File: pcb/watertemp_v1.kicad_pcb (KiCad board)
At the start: 2 copper layers, 56 x 90 mm, 56 parts, among them J1 RN2483 Ext, J2 SWD, J3 I2C, J4 UART1, J5 UART0, Q1 Q_PMOS_GSD, U1 LPC11U24FBD48, U2 RN2483, U3 SHT21, U4 LP5907-Q1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

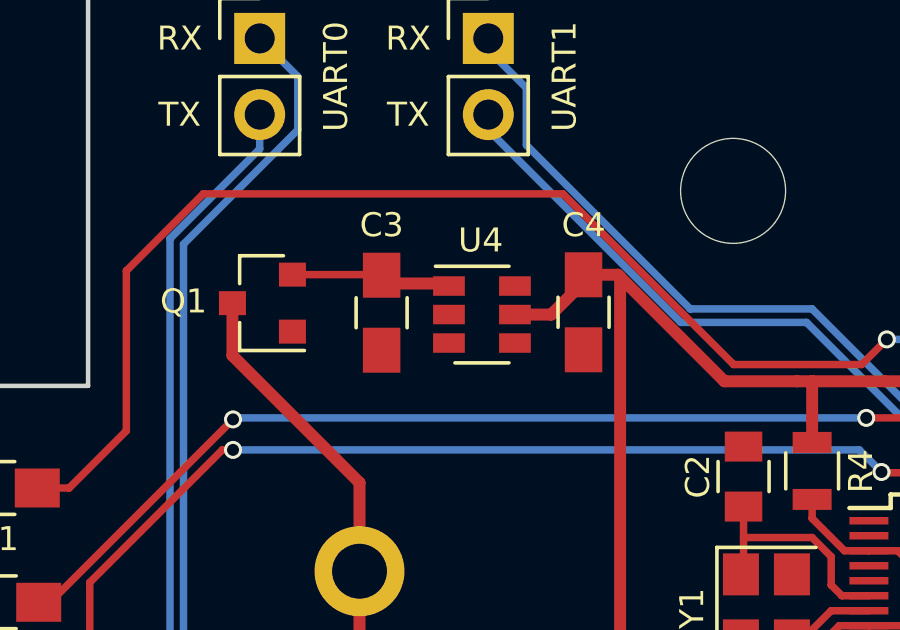
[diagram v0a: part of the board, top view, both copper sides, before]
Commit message: Fix problems with LDO
- Use SOT-23-5 footprint (fixes #9)
- Connect EN to IN
- Connect pin 4 (NC) to GND as recommended in the
  datasheet (section 11.2)
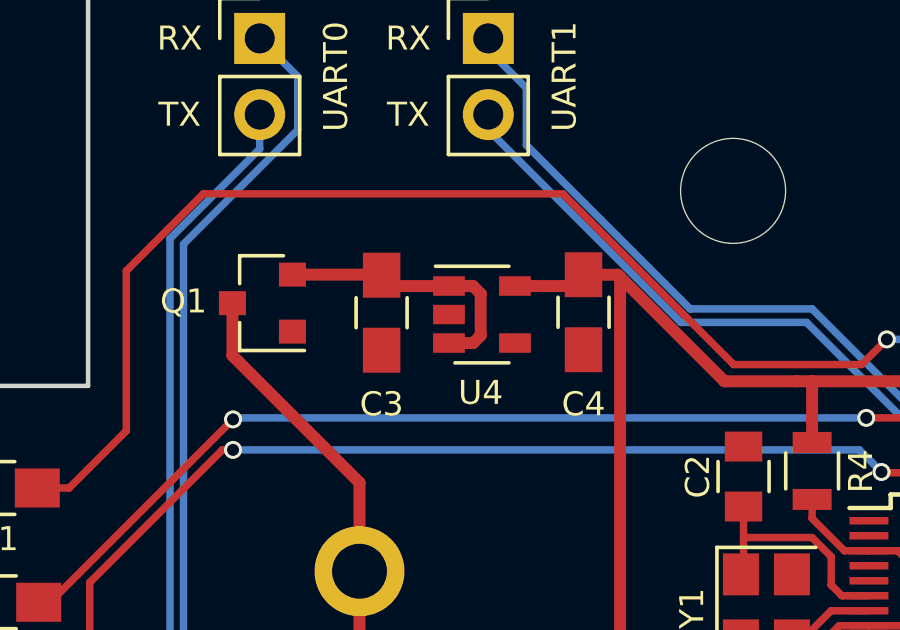
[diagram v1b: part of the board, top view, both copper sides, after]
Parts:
- U4: footprint TO_SOT_Packages_SMD:SOT-23-6 -> TO_SOT_Packages_SMD:SOT-23-5
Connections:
- U4 pad 3: Net-(U4-Pad3) -> Net-(C3-Pad1)
- U4 pad 4: (no net) -> GND
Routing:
- net Net-(C3-Pad1): track 5.35 -> 9.34 mm

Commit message: Routing for voltage divider (fixes #4)
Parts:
- added Q2: Q_DUAL_NMOS_GSD_PMOS_SGD, TSOT_Custom:TSOT26, F.Cu at (63.8, 42.3)
- added R10: 9.30K 0.1%, Resistors_SMD:R_0805, F.Cu at (66.1, 49.3)
- added R11: 10KΩ, Resistors_SMD:R_0805, F.Cu at (68.9, 41.6)
- added R12: 10KΩ, Resistors_SMD:R_0805, F.Cu at (58.1, 43.2)
- added R9: 6.04K 0.1%, Resistors_SMD:R_0805, F.Cu at (66.0, 45.9)
- C3, C4, C5: footprint Capacitors_SMD:C_0805_HandSoldering -> Capacitors_SMD:C_0805
- R1, R2, R3, R6, R7, R8: footprint Resistors_SMD:R_0805_HandSoldering -> Resistors_SMD:R_0805
- moved J4 2.54 mm to (50.8, 42.4)
- moved R1 2.03 mm to (34.9, 57.4)
- moved R2 2.03 mm to (35.0, 61.2)
- moved R3 2.03 mm to (35.0, 65.0)
- moved J5 1.52 mm to (44.2, 42.4)
- moved D1 1.27 mm to (30.7, 57.4)
- moved D3 1.27 mm to (30.7, 65.0)
- moved D2 1.27 mm to (30.7, 61.2)
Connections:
- net Net-(C3-Pad1) renamed VBat
- J2 pad 6: Net-(J2-Pad6) -> (no net)
- J2 pad 7: Net-(J2-Pad7) -> (no net)
- J2 pad 8: Net-(J2-Pad8) -> (no net)
- U1 pad 1: Net-(U1-Pad1) -> (no net)
- U1 pad 10: Net-(U1-Pad10) -> (no net)
- U1 pad 11: Net-(U1-Pad11) -> (no net)
- U1 pad 12: Net-(U1-Pad12) -> (no net)
- U1 pad 13: Net-(U1-Pad13) -> (no net)
- U1 pad 14: Net-(U1-Pad14) -> (no net)
- U1 pad 17: Net-(U1-Pad17) -> (no net)
- U1 pad 18: Net-(U1-Pad18) -> (no net)
- U1 pad 19: Net-(U1-Pad19) -> GND
- U1 pad 2: Net-(U1-Pad2) -> (no net)
- U1 pad 20: Net-(U1-Pad20) -> GND
- U1 pad 21: Net-(U1-Pad21) -> (no net)
- U1 pad 22: Net-(U1-Pad22) -> (no net)
- U1 pad 23: Net-(U1-Pad23) -> (no net)
- U1 pad 24: Net-(U1-Pad24) -> (no net)
- U1 pad 26: Net-(U1-Pad26) -> (no net)
- U1 pad 27: Net-(U1-Pad27) -> (no net)
- U1 pad 28: Net-(U1-Pad28) -> (no net)
- U1 pad 30: Net-(U1-Pad30) -> (no net)
- U1 pad 31: Net-(U1-Pad31) -> (no net)
- U1 pad 32: Net-(U1-Pad32) -> (no net)
- U1 pad 33: Net-(U1-Pad33) -> (no net)
- U1 pad 34: Net-(U1-Pad34) -> (no net)
- U1 pad 35: Net-(U1-Pad35) -> (no net)
- U1 pad 4: Net-(U1-Pad4) -> (no net)
- U1 pad 40: Net-(U1-Pad40) -> (no net)
- U1 pad 42: Net-(U1-Pad42) -> ADC
- U1 pad 43: Net-(U1-Pad43) -> VDivEnable
- U1 pad 9: Net-(U1-Pad9) -> (no net)
- U2 pad 10: Net-(U2-Pad10) -> (no net)
- U2 pad 13: Net-(U2-Pad13) -> (no net)
- U2 pad 14: Net-(U2-Pad14) -> (no net)
- U2 pad 2: Net-(U2-Pad2) -> (no net)
- U2 pad 25: Net-(U2-Pad25) -> (no net)
- U2 pad 3: Net-(U2-Pad3) -> (no net)
- U2 pad 35: Net-(U2-Pad35) -> (no net)
- U2 pad 36: Net-(U2-Pad36) -> (no net)
- U2 pad 37: Net-(U2-Pad37) -> (no net)
- U2 pad 38: Net-(U2-Pad38) -> (no net)
- U2 pad 39: Net-(U2-Pad39) -> (no net)
- U2 pad 4: Net-(U2-Pad4) -> (no net)
- U2 pad 40: Net-(U2-Pad40) -> (no net)
- U2 pad 43: Net-(U2-Pad43) -> (no net)
- U2 pad 44: Net-(U2-Pad44) -> (no net)
- U2 pad 45: Net-(U2-Pad45) -> (no net)
- U2 pad 46: Net-(U2-Pad46) -> (no net)
- U2 pad 5: Net-(U2-Pad5) -> (no net)
- U2 pad 9: Net-(U2-Pad9) -> (no net)
- U3 pad 3: Net-(U3-Pad3) -> (no net)
- U3 pad 4: Net-(U3-Pad4) -> (no net)
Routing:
- net VDivEnable: track 0.00 -> 23.2 mm
- net ADC: track 0.00 -> 16.5 mm, vias 0 -> 2
- net VBat: track 9.34 -> 21.8 mm, vias 0 -> 2
- net Net-(Q2-Pad3): track 0.00 -> 7.18 mm
- net UC-TX1: track 28.8 -> 31.8 mm
- net LED2: track 34.6 -> 37.0 mm
- net LED1: track 47.6 -> 50.0 mm
- net UC-RX1: track 29.9 -> 32.2 mm
- net Net-(Q2-Pad4): track 0.00 -> 2.19 mm
- net LED3: track 34.9 -> 36.7 mm
- net UC-TX0: track 84.4 -> 83.7 mm
- net SCL: track 121.8 -> 122.4 mm
- net 3.3V: track 239.0 -> 238.8 mm, vias 2 -> 4

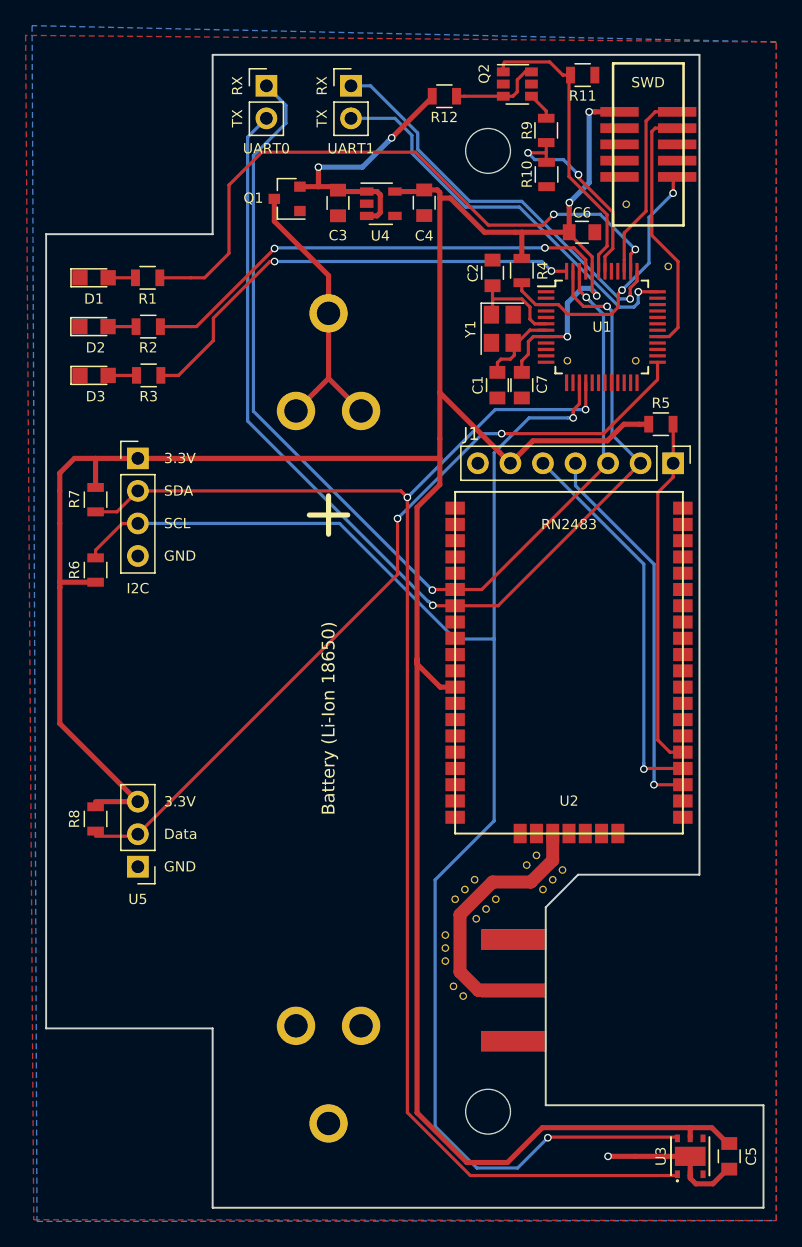
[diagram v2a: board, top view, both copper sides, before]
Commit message: Increase 3.3 supply line thickness
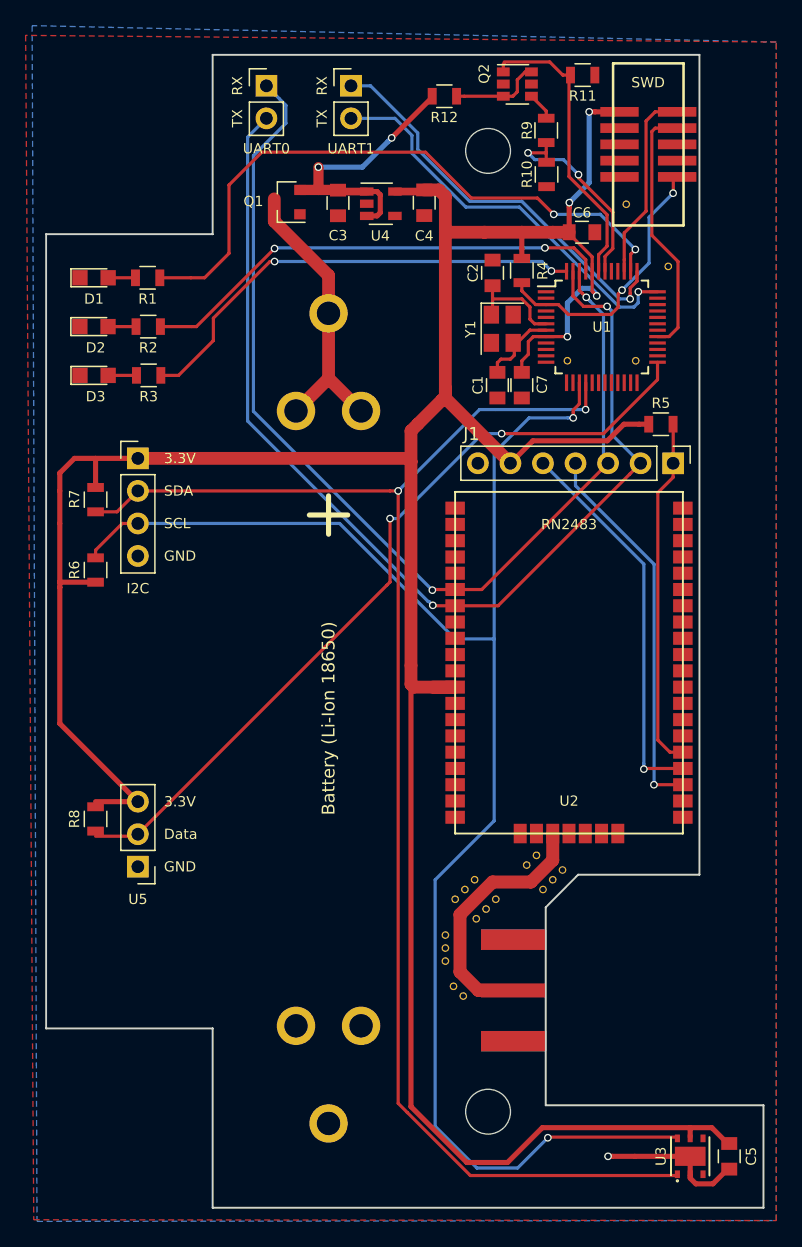
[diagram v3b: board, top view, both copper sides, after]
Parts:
- moved Q1 0.25 mm to (45.8, 51.5)
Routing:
- net 3.3V: track 238.8 -> 237.8 mm
- net LED1: track 50.0 -> 49.3 mm

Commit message: Connect remaining unconnected parts
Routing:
- net VBat: track 22.1 -> 28.5 mm
- net UC-TX1: track 31.8 -> 32.5 mm
- net UC-RX1: track 32.2 -> 32.8 mm
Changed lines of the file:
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@@
   (general
     (links 136)
-    (no_connects 3)
+    (no_connects 0)
     (area 22.966905 37.719 91.100001 131.826001)
     (thickness 1.6)
     (drawings 32)
-    (tracks 394)
+    (tracks 401)
     (zones 0)
     (modules 61)
@@
   )
   (module RN2483:RN2483 (layer F.Cu)
-    (at 67.818 87.4522 180)
+    (at 67.818 87.445 180)
     (tags rn2483,lora,lorawan)
     (fp_text reference U2 (at 0 -10.795 180) (layer F.SilkS)
@@
   (segment (start 61.849 59.055) (end 61.849 58.023) (width 0.25) (layer F.Cu) (net 5))
   (segment (start 61.849 60.284) (end 61.849 59.055) (width 0.25) (layer F.Cu) (net 5))
+  (segment (start 30.861 98.698) (end 33.763 98.698) (width 0.4) (layer F.Cu) (net 6))
+  (segment (start 33.763 98.698) (end 34.163 98.298) (width 0.4) (layer F.Cu) (net 6))
   (segment (start 77.2414 123.7488) (end 65.7352 123.7488) (width 0.4) (layer F.Cu) (net 6))
   (segment (start 65.7352 123.7488) (end 63.0174 126.4666) (width 0.4) (layer F.Cu) (net 6))
@@
   (segment (start 65.032998 61.996) (end 66.028 61.996) (width 0.25) (layer F.Cu) (net 6))
   (segment (start 66.548 53.848) (end 67.834 53.848) (width 1) (layer F.Cu) (net 6))
-  (segment (start 30.861 98.298) (end 34.163 98.298) (width 0.4) (layer F.Cu) (net 6))
   (segment (start 34.0106 98.1456) (end 34.163 98.298) (width 0.4) (layer F.Cu) (net 6))
   (segment (start 28.067 81.5721) (end 28.067 92.202) (width 0.4) (layer F.Cu) (net 6))
@@
   (segment (start 66.216999 124.484) (end 66.167 124.533999) (width 0.25) (layer F.Cu) (net 16))
   (via (at 66.167 124.533999) (size 0.6) (drill 0.4) (layers F.Cu B.Cu) (net 16))
-  (segment (start 56.007 46.101) (end 52.324 42.418) (width 0.25) (layer B.Cu) (net 17))
-  (segment (start 52.324 42.418) (end 50.8 42.418) (width 0.25) (layer B.Cu) (net 17))
-  (segment (start 60.071 51.435) (end 56.007 47.371) (width 0.25) (layer B.Cu) (net 17))
-  (segment (start 56.007 47.371) (end 56.007 46.101) (width 0.25) (layer B.Cu) (net 17))
   (segment (start 72.5932 59.055) (end 71.755 59.055) (width 0.25) (layer B.Cu) (net 17))
   (segment (start 71.755 59.055) (end 64.135 51.435) (width 0.25) (layer B.Cu) (net 17))
+  (segment (start 53.418 42.418) (end 50.8 42.418) (width 0.25) (layer B.Cu) (net 17))
   (segment (start 64.135 51.435) (end 60.071 51.435) (width 0.25) (layer B.Cu) (net 17))
+  (segment (start 57 48.364) (end 57 46) (width 0.25) (layer B.Cu) (net 17))
+  (segment (start 60.071 51.435) (end 57 48.364) (width 0.25) (layer B.Cu) (net 17))
+  (segment (start 57 46) (end 53.418 42.418) (width 0.25) (layer B.Cu) (net 17))
   (segment (start 50.8 42.799) (end 50.8 42.418) (width 0.25) (layer B.Cu) (net 17))
   (segment (start 72.5932 58.206198) (end 72.5932 58.630736) (width 0.25) (layer F.Cu) (net 17))
@@
   (via (at 72.5932 59.055) (size 0.6) (drill 0.4) (layers F.Cu B.Cu) (net 17))
   (segment (start 72.5932 58.630736) (end 72.5932 59.055) (width 0.25) (layer F.Cu) (net 17))
-  (segment (start 50.8 44.958) (end 54.22759 44.958) (width 0.25) (layer B.Cu) (net 18))
-  (segment (start 54.22759 44.958) (end 55.55699 46.2874) (width 0.25) (layer B.Cu) (net 18))
-  (segment (start 55.55699 46.2874) (end 55.55699 47.68299) (width 0.25) (layer B.Cu) (net 18))
-  (segment (start 59.75901 51.88501) (end 63.9486 51.88501) (width 0.25) (layer B.Cu) (net 18))
-  (segment (start 73.218201 58.506199) (end 73.2282 58.4962) (width 0.25) (layer B.Cu) (net 18))
-  (segment (start 55.55699 47.68299) (end 59.75901 51.88501) (width 0.25) (layer B.Cu) (net 18))
-  (segment (start 63.9486 51.88501) (end 71.75359 59.69) (width 0.25) (layer B.Cu) (net 18))
-  (segment (start 71.75359 59.69) (end 72.883202 59.69) (width 0.25) (layer B.Cu) (net 18))
-  (segment (start 72.883202 59.69) (end 73.218201 59.355001) (width 0.25) (layer B.Cu) (net 18))
-  (segment (start 73.218201 59.355001) (end 73.218201 58.506199) (width 0.25) (layer B.Cu) (net 18))
+  (segment (start 73.2282 58.4962) (end 73.218201 58.506199) (width 0.25) (layer B.Cu) (net 18))
+  (segment (start 73.218201 58.506199) (end 73.218201 59.355001) (width 0.25) (layer B.Cu) (net 18))
+  (segment (start 73.218201 59.355001) (end 72.883202 59.69) (width 0.25) (layer B.Cu) (net 18))
+  (segment (start 56.5 48.626) (end 56.5 46.13641) (width 0.25) (layer B.Cu) (net 18))
+  (segment (start 72.883202 59.69) (end 71.75359 59.69) (width 0.25) (layer B.Cu) (net 18))
+  (segment (start 71.75359 59.69) (end 63.9486 51.88501) (width 0.25) (layer B.Cu) (net 18))
+  (segment (start 63.9486 51.88501) (end 59.75901 51.88501) (width 0.25) (layer B.Cu) (net 18))
+  (segment (start 56.5 46.13641) (end 55.32159 44.958) (width 0.25) (layer B.Cu) (net 18))
+  (segment (start 59.75901 51.88501) (end 56.5 48.626) (width 0.25) (layer B.Cu) (net 18))
+  (segment (start 55.32159 44.958) (end 50.8 44.958) (width 0.25) (layer B.Cu) (net 18))
   (segment (start 74.728 58.496) (end 73.2284 58.496) (width 0.25) (layer F.Cu) (net 18))
   (segment (start 73.2284 58.496) (end 73.2282 58.4962) (width 0.25) (layer F.Cu) (net 18))
@@
   (segment (start 66.4718 56.896) (end 66.4464 56.8706) (width 0.25) (layer F.Cu) (net 21))
   (via (at 66.4464 56.8706) (size 0.6) (drill 0.4) (layers F.Cu B.Cu) (net 21))
+  (segment (start 30.861 100.598) (end 33.923 100.598) (width 0.25) (layer F.Cu) (net 22))
+  (segment (start 33.923 100.598) (end 34.163 100.838) (width 0.25) (layer F.Cu) (net 22))
   (segment (start 34.163 100.838) (end 53.594 81.407) (width 0.25) (layer F.Cu) (net 22))
   (segment (start 53.848 76.2) (end 53.848 81.153) (width 0.25) (layer F.Cu) (net 22))
@@
   (segment (start 61.0616 69.5706) (end 54.4322 76.2) (width 0.25) (layer B.Cu) (net 22))
   (segment (start 54.4322 76.2) (end 53.848 76.2) (width 0.25) (layer B.Cu) (net 22))
-  (segment (start 30.861 100.998) (end 34.003 100.998) (width 0.25) (layer F.Cu) (net 22))
   (segment (start 34.003 100.998) (end 34.163 100.838) (width 0.25) (layer F.Cu) (net 22))
   (segment (start 34.1554 100.8456) (end 34.163 100.838) (width 0.25) (layer F.Cu) (net 22))
@@
   (segment (start 31.834 61.214) (end 34.022 61.214) (width 0.25) (layer F.Cu) (net 24))
   (segment (start 31.8418 65.024) (end 34.055 65.024) (width 0.25) (layer F.Cu) (net 25))
+  (segment (start 54 46.5) (end 54.5 46) (width 0.4) (layer B.Cu) (net 26))
+  (segment (start 54 46.5) (end 51.732 48.768) (width 0.4) (layer B.Cu) (net 26))
+  (segment (start 57.1398 43.2308) (end 57.1398 42.9308) (width 0.4) (layer F.Cu) (net 26))
+  (segment (start 57.989799 42.080801) (end 61.587201 42.080801) (width 0.4) (layer F.Cu) (net 26))
+  (segment (start 57.1398 42.9308) (end 57.989799 42.080801) (width 0.4) (layer F.Cu) (net 26))
+  (segment (start 61.587201 42.080801) (end 61.7872 42.2808) (width 0.4) (layer F.Cu) (net 26))
+  (segment (start 61.7872 42.2808) (end 62.6872 42.2808) (width 0.4) (layer F.Cu) (net 26))
+  (segment (start 57.1398 43.2308) (end 57.1398 43.3602) (width 0.4) (layer F.Cu) (net 26))
+  (segment (start 57.1398 43.3602) (end 54.5 46) (width 0.4) (layer F.Cu) (net 26))
+  (segment (start 51.732 48.768) (end 48.26 48.768) (width 0.4) (layer B.Cu) (net 26))
   (segment (start 46.8122 50.546) (end 48.26 50.546) (width 0.8) (layer F.Cu) (net 26))
   (segment (start 48.26 50.546) (end 49.768 50.546) (width 0.8) (layer F.Cu) (net 26))
-  (segment (start 48.26 48.768) (end 48.26 50.546) (width 0.8) (layer F.Cu) (net 26))
+  (segment (start 48.26 48.768) (end 48.26 50.546) (width 0.6) (layer F.Cu) (net 26))
   (segment (start 49.768 50.546) (end 49.784 50.562) (width 0.4) (layer F.Cu) (net 26))
-  (segment (start 53.975 46.481998) (end 57.1398 43.317198) (width 0.4) (layer F.Cu) (net 26))
   (segment (start 57.1398 43.317198) (end 57.1398 43.2308) (width 0.4) (layer F.Cu) (net 26))
-  (segment (start 53.975002 46.481998) (end 53.975 46.481998) (width 0.4) (layer F.Cu) (net 26))
-  (segment (start 51.688998 48.768) (end 53.675001 46.781997) (width 0.4) (layer B.Cu) (net 26))
-  (segment (start 48.26 48.768) (end 51.688998 48.768) (width 0.4) (layer B.Cu) (net 26))
-  (segment (start 53.675001 46.781997) (end 53.975 46.481998) (width 0.4) (layer B.Cu) (net 26))
-  (via (at 53.975 46.481998) (size 0.6) (drill 0.4) (layers F.Cu B.Cu) (net 26))
+  (via (at 54.5 46) (size 0.6) (drill 0.4) (layers F.Cu B.Cu) (net 26))
   (via (at 48.26 48.768) (size 0.6) (drill 0.4) (layers F.Cu B.Cu) (net 26))
   (segment (start 52.029 50.673) (end 50.145 50.673) (width 0.6) (layer F.Cu) (net 26))
